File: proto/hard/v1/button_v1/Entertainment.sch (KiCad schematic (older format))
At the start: 44 parts, among them J6 Conn_01x08_Female, J8 AudioJack3, Q2 IRLML2060, Q4 IRLML2060, Q5 IRLML2060, U10 NL27WZ14, U5 RT9293, U8 485, U9 LM358

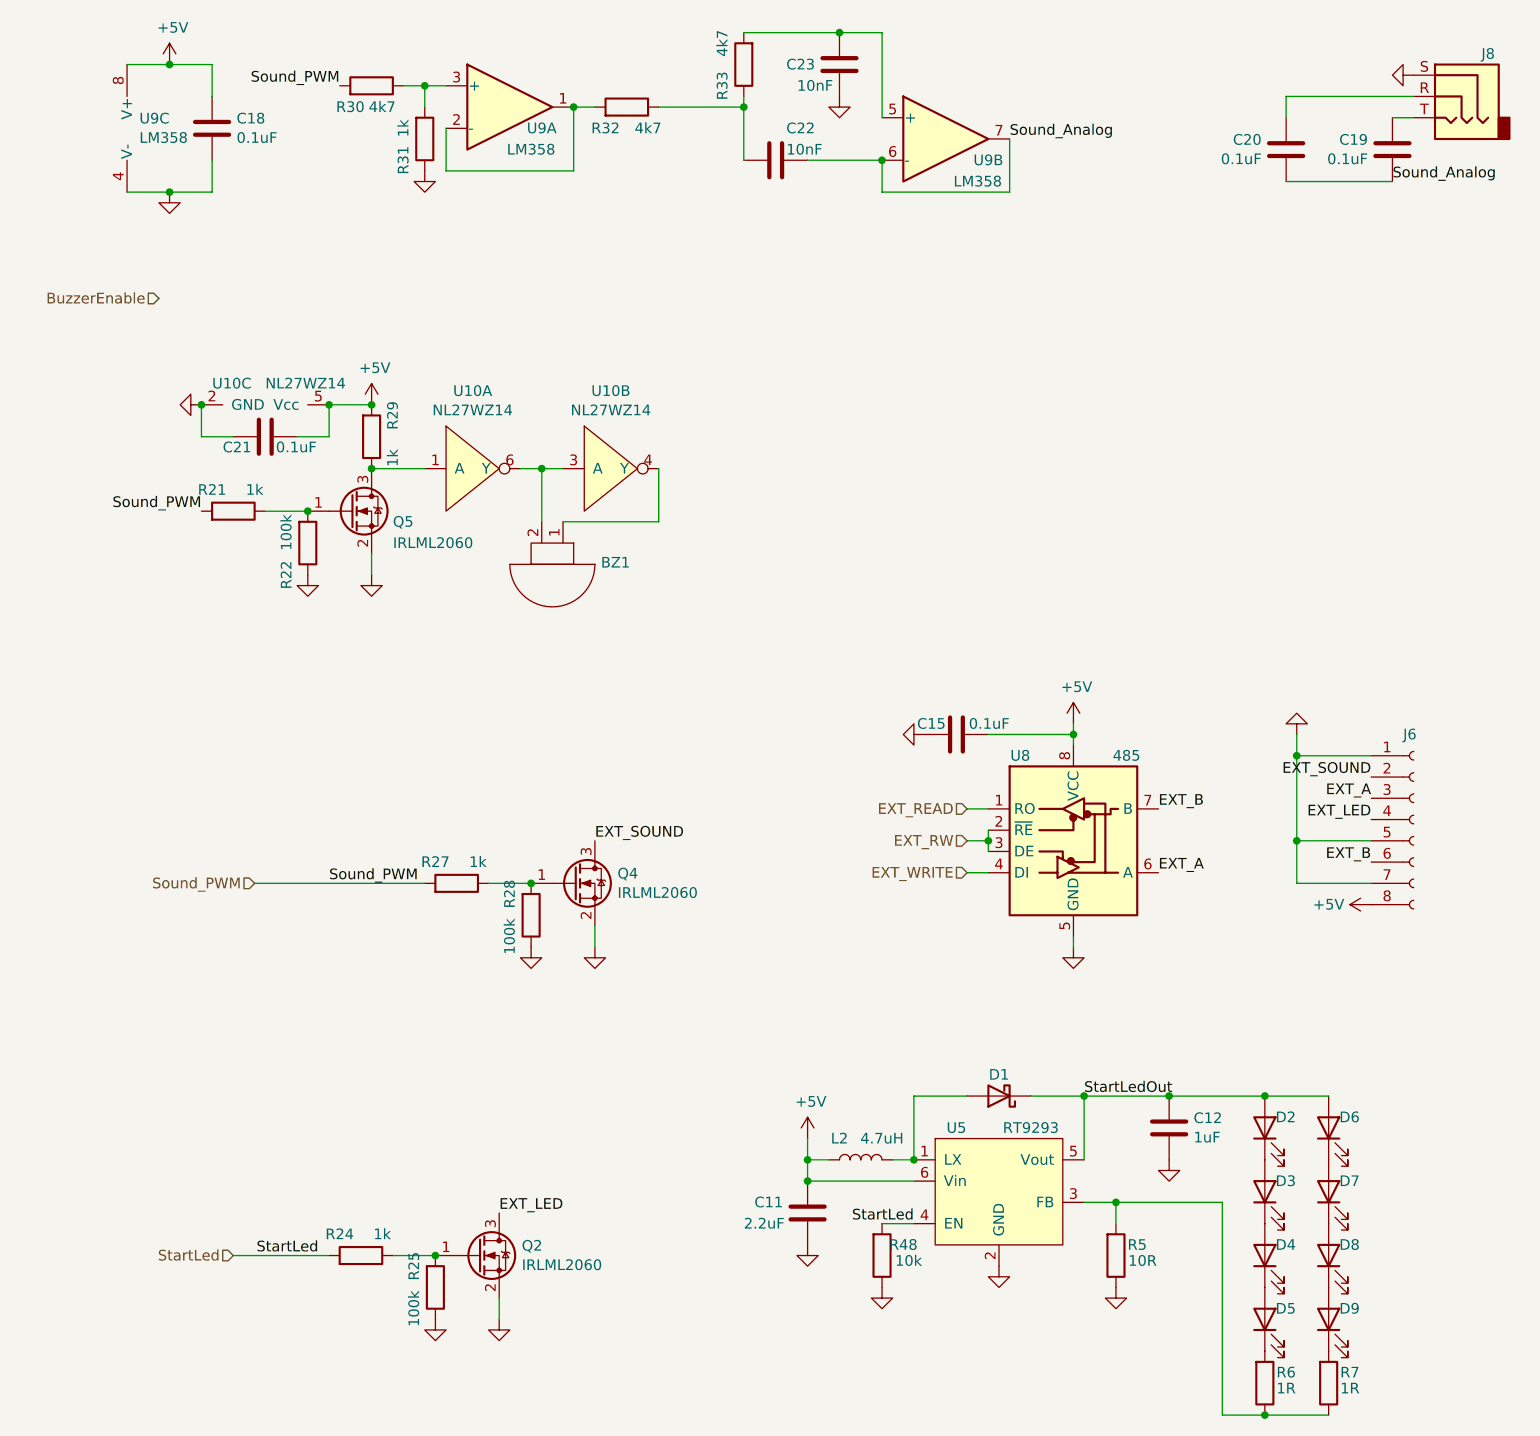
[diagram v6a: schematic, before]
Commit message: Moved buttons to separate sheet. Added replacement transistors for buttons.
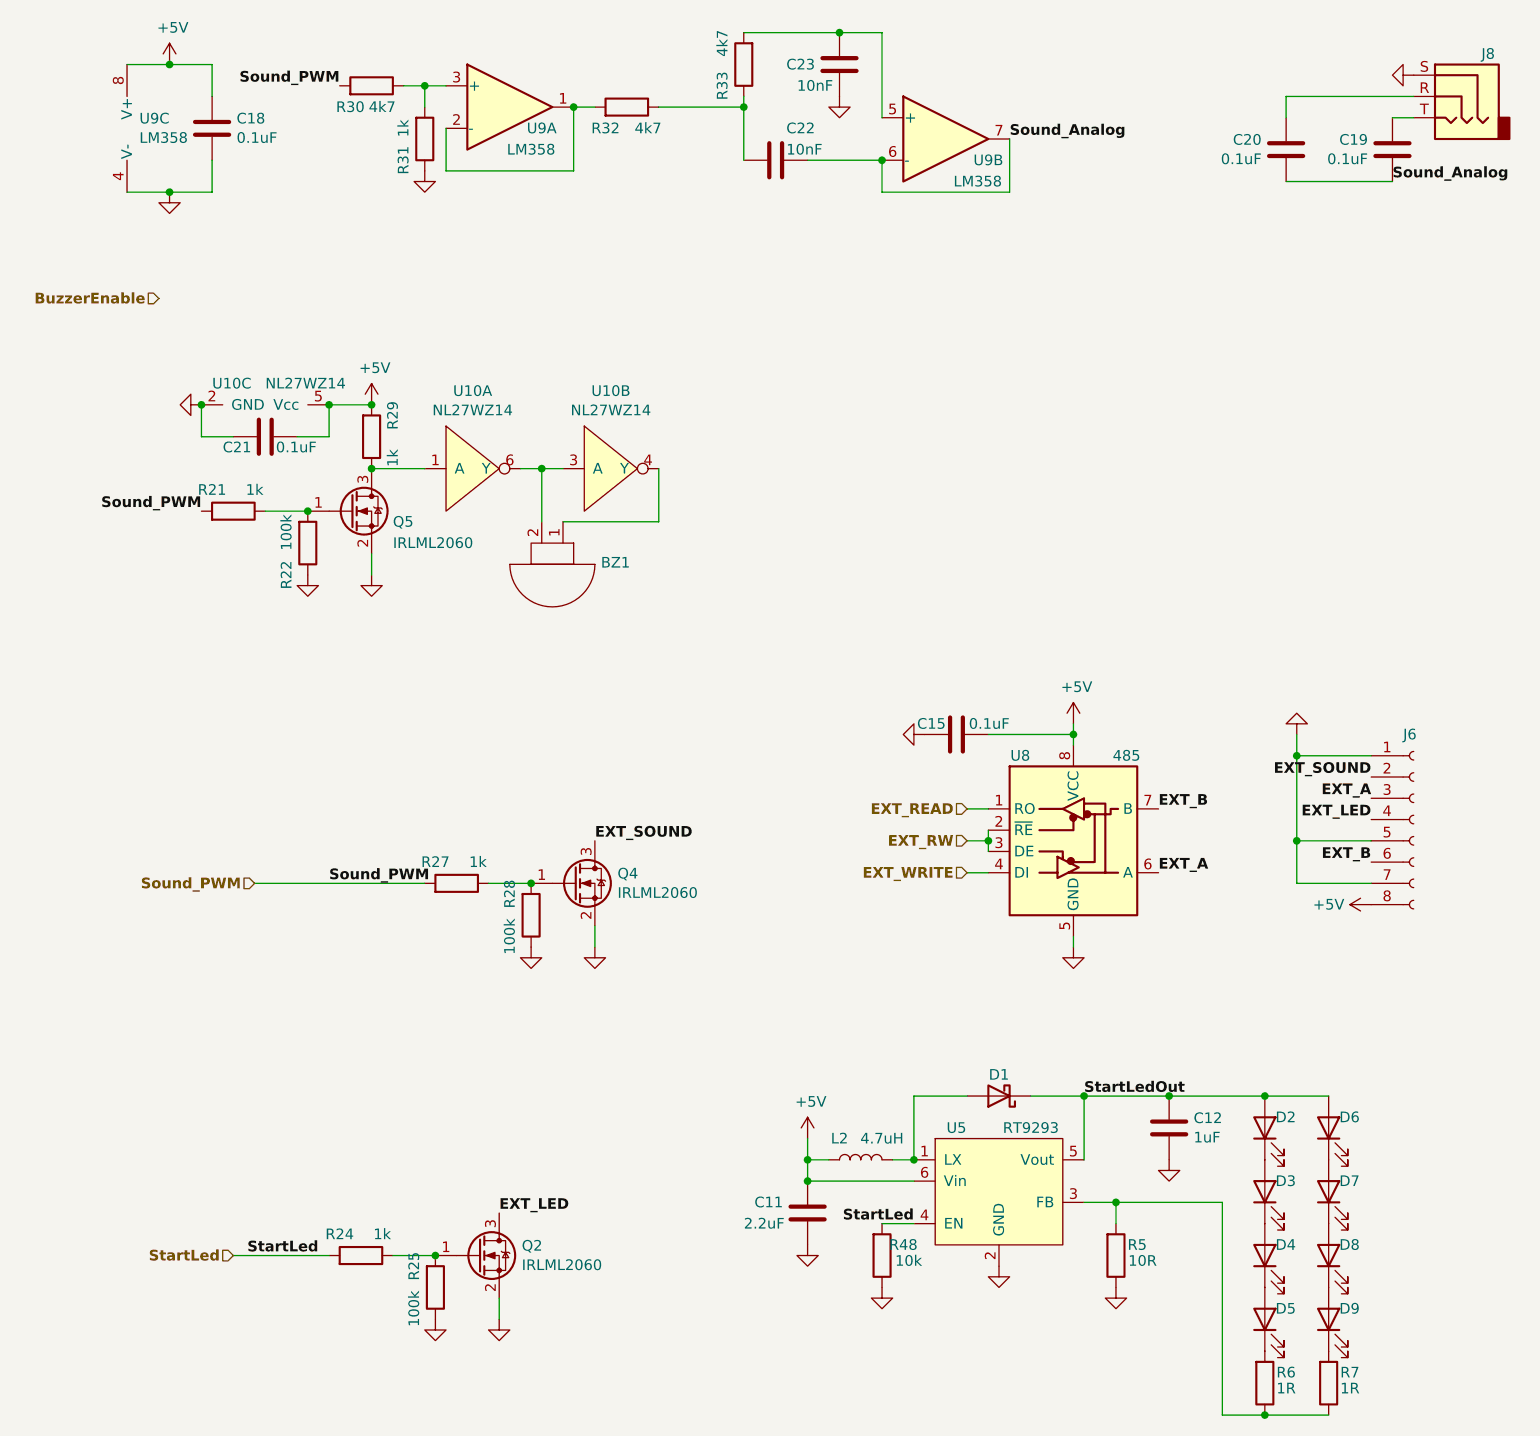
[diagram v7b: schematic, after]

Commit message: BOOT0 connected to GND Due to migration to Kicad V5.1.6 had to change text style from "bold" to "normal"
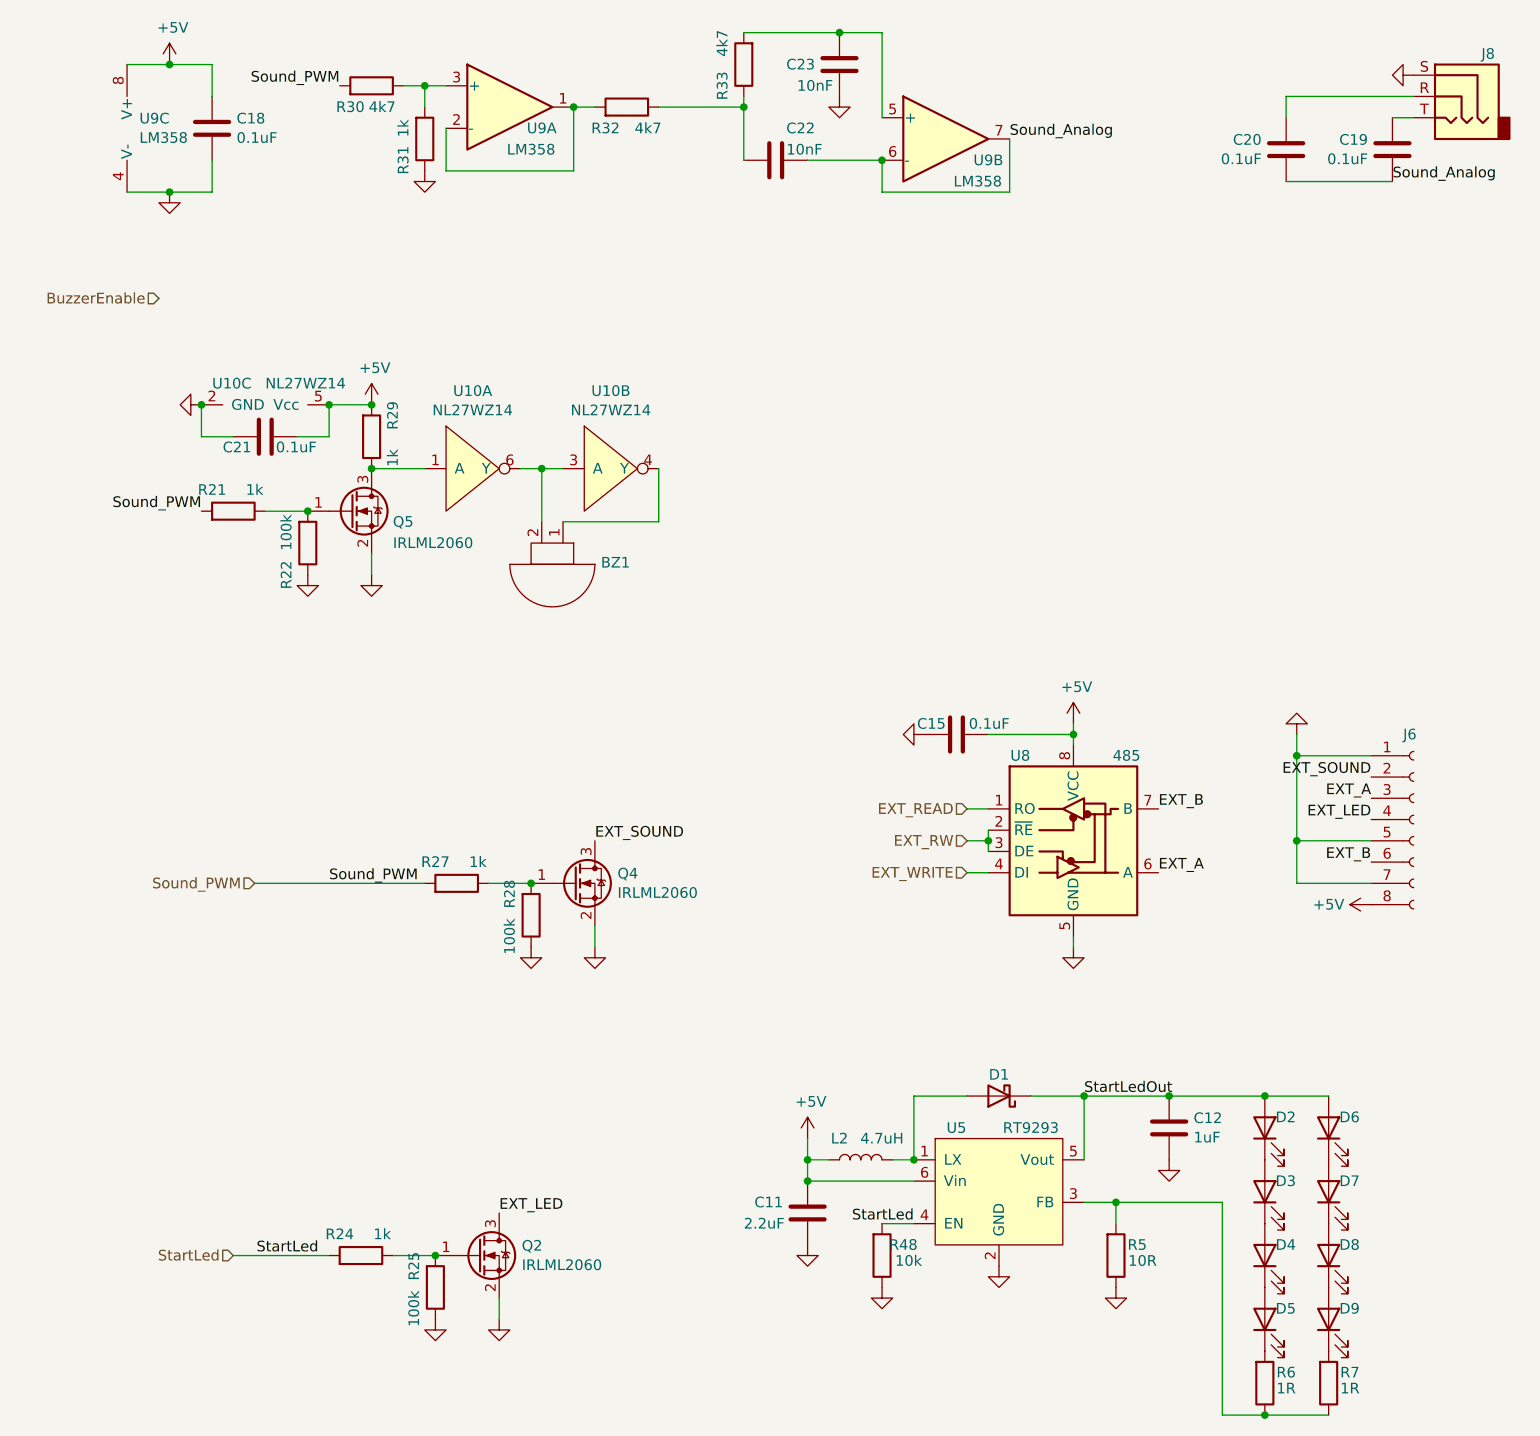
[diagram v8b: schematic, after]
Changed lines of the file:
@@
 EESchema Schematic File Version 4
-LIBS:button_v1-cache
-EELAYER 29 0
+EELAYER 30 0
 EELAYER END
 $Descr A4 11693 8268
@@
 	1    0    0    -1
 $EndComp
-Text Label 6800 4850 2    50   ~ 6
+Text Label 6800 4850 2    50   ~ 0
 EXT_B
-Text Label 6800 4550 2    50   ~ 6
+Text Label 6800 4550 2    50   ~ 0
 EXT_A
-Text Label 6800 4650 2    50   ~ 6
+Text Label 6800 4650 2    50   ~ 0
 EXT_LED
 $Comp
@@
 Wire Wire Line
 	6800 4350 6450 4350
-Text Label 6800 4450 2    50   ~ 6
+Text Label 6800 4450 2    50   ~ 0
 EXT_SOUND
 Wire Wire Line
@@
 	1    0    0    -1
 $EndComp
-Text Label 5800 4600 0    50   ~ 6
+Text Label 5800 4600 0    50   ~ 0
 EXT_B
 Wire Wire Line
@@
 	1    0    0    -1
 $EndComp
-Text Label 5800 4900 0    50   ~ 6
+Text Label 5800 4900 0    50   ~ 0
 EXT_A
 Wire Wire Line
@@
 	0    -1   -1   0
 $EndComp
-Text HLabel 4900 4600 0    50   Input ~ 6
+Text HLabel 4900 4600 0    50   Input ~ 0
 EXT_READ
 $Comp
@@
 Wire Wire Line
 	4900 4600 5000 4600
-Text HLabel 4900 4750 0    50   Input ~ 6
+Text HLabel 4900 4750 0    50   Input ~ 0
 EXT_RW
 Wire Wire Line
@@
 Wire Wire Line
 	5000 4750 5000 4700
-Text HLabel 4900 4900 0    50   Input ~ 6
+Text HLabel 4900 4900 0    50   Input ~ 0
 EXT_WRITE
 Wire Wire Line
@@
 Wire Wire Line
 	2200 6700 2400 6700
-Text Label 2700 6500 0    50   ~ 6
+Text Label 2700 6500 0    50   ~ 0
 EXT_LED
-Text HLabel 1450 6700 0    50   Input ~ 6
+Text HLabel 1450 6700 0    50   Input ~ 0
 StartLed
 Wire Wire Line
@@
 Wire Wire Line
 	3150 5150 3150 5250
-Text Label 3150 4750 0    50   ~ 6
+Text Label 3150 4750 0    50   ~ 0
 EXT_SOUND
 $Comp
@@
 Wire Wire Line
 	2650 4950 2850 4950
-Text HLabel 1550 4950 0    50   Input ~ 6
+Text HLabel 1550 4950 0    50   Input ~ 0
 Sound_PWM
 Wire Wire Line
@@
 	1    0    0    -1
 $EndComp
-Text Label 1300 3200 2    50   ~ 6
+Text Label 1300 3200 2    50   ~ 0
 Sound_PWM
 $Comp
@@
 	1    0    0    -1
 $EndComp
-Text Label 1900 4950 0    50   ~ 6
+Text Label 1900 4950 0    50   ~ 0
 Sound_PWM
-Text Label 5450 5950 0    50   ~ 6
+Text Label 5450 5950 0    50   ~ 0
 StartLedOut
 $Comp
@@
 	0    -1   -1   0
 $EndComp
-Text Label 4650 6550 2    50   ~ 6
+Text Label 4650 6550 2    50   ~ 0
 StartLed
 $Comp
@@
 	1    0    0    -1
 $EndComp
-Text Label 1850 6700 2    50   ~ 6
+Text Label 1850 6700 2    50   ~ 0
 StartLed
-Text Label 6900 1650 0    50   ~ 6
+Text Label 6900 1650 0    50   ~ 0
 Sound_Analog
 Wire Wire Line
@@
 	0    1    -1   0
 $EndComp
-Text Label 5100 1450 0    50   ~ 6
+Text Label 5100 1450 0    50   ~ 0
 Sound_Analog
-Text Label 1950 1200 2    50   ~ 6
+Text Label 1950 1200 2    50   ~ 0
 Sound_PWM
 Wire Wire Line
@@
 Wire Wire Line
 	4650 6550 4500 6550
-Text HLabel 1100 2200 0    50   Input ~ 6
+Text HLabel 1100 2200 0    50   Input ~ 0
 BuzzerEnable
 Wire Wire Line
